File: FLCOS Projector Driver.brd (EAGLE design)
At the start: 73.9 x 62.1 mm, 62 parts, among them IC2 LM3414, IC3 MIC5219BM5, IC4 MIC5219BM5, IC5 LM3414, IC6 LM3414, Q1 14.31818MHz, Q3 12MHz, T2 S8050, T3 S8050, U1 TVP5150-NTSC_DECODER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

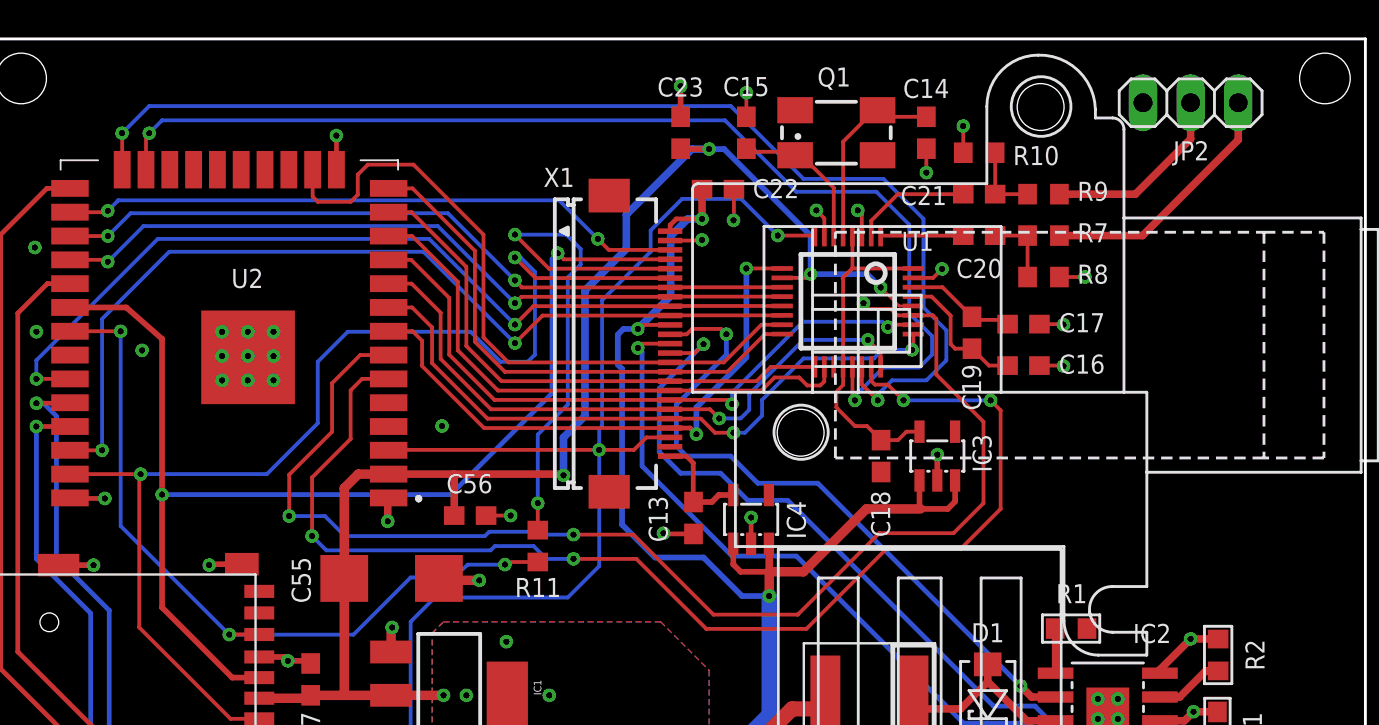
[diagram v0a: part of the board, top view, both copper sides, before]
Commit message: added pullups to I2C
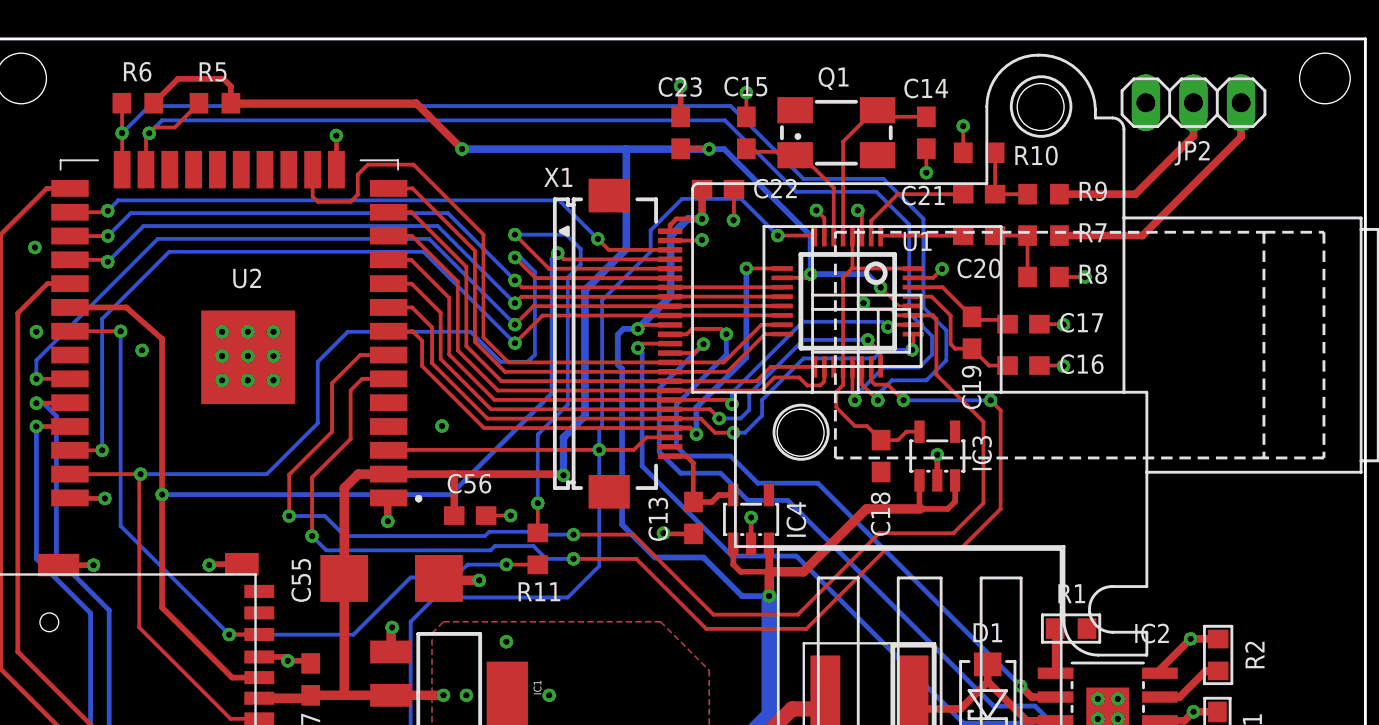
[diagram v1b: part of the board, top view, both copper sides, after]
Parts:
- added R5, R6: 2K2, rcl:R0603
- moved JP2 0.15 mm to (69.1, 62.5)
- moved R11 0.15 mm to (34.1, 38.7), turned to 90 degrees
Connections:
- net +3V3: now also R5.2, R6.2
- net FLCOS_SOUT: now also R11.2; no longer R11.1
- net SPI_MISO: now also R11.1; no longer R11.2
- net TVP_SCL: now also R5.1
- net TVP_SDA: now also R6.1
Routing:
- net +3V3: track 79.9 -> 109.8 mm, vias 9 -> 10
- net TVP_SCL: track 59.8 -> 63.0 mm
- net TVP_SDA: track 62.7 -> 64.3 mm
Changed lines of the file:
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@@
 <attribute name="OC_NEWARK" value="unknown" x="50.0634" y="60.9092" size="1.778" layer="27" display="off"/>
 </element>
-<element name="JP2" library="pinhead" package="1X03" package3d_urn="urn:adsk.eagle:package:22458/2" value="" x="68.961" y="62.5094" smashed="yes" rot="R180">
-<attribute name="NAME" x="69.9516" y="60.452" size="1.016" layer="25" ratio="10" rot="R180"/>
-<attribute name="VALUE" x="72.771" y="65.6844" size="1.27" layer="27" rot="R180"/>
+<element name="JP2" library="pinhead" package="1X03" package3d_urn="urn:adsk.eagle:package:22458/2" value="" x="69.1134" y="62.5094" smashed="yes" rot="R180">
+<attribute name="NAME" x="70.104" y="60.452" size="1.016" layer="25" ratio="10" rot="R180"/>
+<attribute name="VALUE" x="72.9234" y="65.6844" size="1.27" layer="27" rot="R180"/>
 </element>
 <element name="C22" library="rcl" package="C0603" value="100nF" x="43.7506" y="57.8984" smashed="yes" rot="R180">
@@
 <attribute name="VALUE" x="43.6118" y="37.1094" size="1.016" layer="27"/>
 </element>
-<element name="R11" library="rcl" package="R0603" value="0R" x="34.1376" y="38.862" smashed="yes" rot="R270">
-<attribute name="NAME" x="35.3822" y="37.1602" size="1.016" layer="25" rot="R180"/>
-<attribute name="VALUE" x="32.2326" y="39.497" size="1.27" layer="27" rot="R270"/>
-</element>
 <element name="IC1" library="SparkFun" package="SOT223" value="" x="29.4132" y="30.9" rot="R270"/>
 <element name="RGB" library="con-jst" package="ZH-8" value="ZH-8" x="39.0144" y="18.161" smashed="yes" rot="R270">
@@
 <attribute name="NAME" x="67.2846" y="15.554" size="1.016" layer="25" ratio="12" align="bottom-center"/>
 <attribute name="VALUE" x="64.5414" y="14.9444" size="0.5" layer="27" font="vector" ratio="12" rot="R180" align="top-center"/>
+</element>
+<element name="R11" library="rcl" package="R0603" value="0R" x="34.1376" y="38.7096" smashed="yes" rot="R90">
+<attribute name="NAME" x="35.4584" y="36.9316" size="1.016" layer="25" rot="R180"/>
+<attribute name="VALUE" x="36.0426" y="38.0746" size="1.27" layer="27" rot="R90"/>
+</element>
+<element name="R5" library="rcl" package="R0603" value="2K2" x="16.9164" y="62.484" smashed="yes">
+<attribute name="NAME" x="15.9766" y="63.6524" size="1.016" layer="25"/>
+<attribute name="VALUE" x="16.2814" y="60.579" size="1.27" layer="27"/>
+</element>
+<element name="R6" library="rcl" package="R0603" value="2K2" x="12.8016" y="62.484" smashed="yes">
+<attribute name="NAME" x="11.938" y="63.6524" size="1.016" layer="25"/>
+<attribute name="VALUE" x="12.1666" y="60.579" size="1.27" layer="27"/>
 </element>
 </elements>
@@
 <wire x1="50.923" y1="46.7654" x2="51.054" y2="46.6344" width="0.2032" layer="1"/>
 <via x="51.054" y="46.6344" extent="1-16" drill="0.3302"/>
-<wire x1="13.239" y1="58.9392" x2="13.239" y2="60.864" width="0.2032" layer="1"/>
-<wire x1="13.239" y1="60.864" x2="13.4112" y2="60.8838" width="0.2032" layer="1"/>
+<wire x1="13.239" y1="58.9392" x2="13.239" y2="60.7116" width="0.2032" layer="1"/>
+<wire x1="13.239" y1="60.7116" x2="13.4112" y2="60.8838" width="0.2032" layer="1"/>
 <via x="13.4112" y="60.8838" extent="1-16" drill="0.3302"/>
 <wire x1="52.197" y1="57.7596" x2="47.9298" y2="57.7596" width="0.2032" layer="16"/>
@@
 <wire x1="54.483" y1="48.387" x2="52.578" y2="48.387" width="0.2032" layer="16"/>
 <wire x1="52.578" y1="48.387" x2="51.054" y2="46.863" width="0.2032" layer="16"/>
+<contactref element="R5" pad="1"/>
+<wire x1="13.4112" y1="60.8838" x2="13.716" y2="61.1886" width="0.2032" layer="1"/>
+<wire x1="13.716" y1="61.1886" x2="14.771" y2="61.1886" width="0.2032" layer="1"/>
+<wire x1="14.771" y1="61.1886" x2="16.0664" y2="62.484" width="0.2032" layer="1"/>
 </signal>
 <signal name="TVP_SDA">
@@
 <wire x1="54.864" y1="47.7012" x2="53.0352" y2="47.7012" width="0.2032" layer="16"/>
 <wire x1="53.0352" y1="47.7012" x2="52.2732" y2="46.9392" width="0.2032" layer="16"/>
+<contactref element="R6" pad="1"/>
+<wire x1="11.9634" y1="60.8838" x2="11.9634" y2="62.4722" width="0.2032" layer="1"/>
+<wire x1="11.9634" y1="62.4722" x2="11.9516" y2="62.484" width="0.2032" layer="1"/>
 </signal>
 <signal name="XTAL1">
@@
 <via x="32.9184" y="55.4736" extent="1-16" drill="0.3302"/>
 <via x="34.1376" y="41.148" extent="1-16" drill="0.3302"/>
-<contactref element="R11" pad="1"/>
 <wire x1="34.735" y1="53.657" x2="32.9184" y2="55.4736" width="0.2032" layer="1"/>
 <wire x1="41.1976" y1="53.657" x2="34.735" y2="53.657" width="0.2032" layer="1"/>
 <wire x1="32.9184" y1="55.4736" x2="35.6616" y2="55.4736" width="0.2032" layer="16"/>
 <wire x1="36.4236" y1="54.7116" x2="35.6616" y2="55.4736" width="0.2032" layer="16"/>
-<wire x1="34.1376" y1="39.712" x2="34.1376" y2="41.148" width="0.2032" layer="1"/>
 <wire x1="36.4236" y1="53.8734" x2="36.4236" y2="54.7116" width="0.2032" layer="16"/>
 <wire x1="35.7378" y1="53.1876" x2="35.7378" y2="46.4058" width="0.2032" layer="16"/>
@@
 <wire x1="35.7378" y1="46.4058" x2="34.1376" y2="44.8056" width="0.2032" layer="16"/>
 <wire x1="34.1376" y1="44.8056" x2="34.1376" y2="41.148" width="0.2032" layer="16"/>
+<contactref element="R11" pad="2"/>
+<wire x1="34.1376" y1="39.5596" x2="34.1376" y2="41.148" width="0.2032" layer="1"/>
 </signal>
 <signal name="SPI_MOSI">
@@
 <contactref element="JP2" pad="1"/>
 <wire x1="61.9624" y1="55.4228" x2="66.3956" y2="55.4228" width="0.4064" layer="1"/>
-<wire x1="71.501" y1="60.5282" x2="71.501" y2="62.5094" width="0.4064" layer="1"/>
-<wire x1="66.3956" y1="55.4228" x2="71.501" y2="60.5282" width="0.4064" layer="1"/>
+<wire x1="71.6534" y1="60.6806" x2="71.6534" y2="62.5094" width="0.4064" layer="1"/>
+<wire x1="66.3956" y1="55.4228" x2="71.6534" y2="60.6806" width="0.4064" layer="1"/>
 </signal>
 <signal name="N$21">
@@
 <contactref element="JP2" pad="2"/>
 <wire x1="61.9624" y1="57.6326" x2="66.0146" y2="57.6326" width="0.4064" layer="1"/>
-<wire x1="68.961" y1="60.579" x2="68.961" y2="62.5094" width="0.4064" layer="1"/>
-<wire x1="66.0146" y1="57.6326" x2="68.961" y2="60.579" width="0.4064" layer="1"/>
+<wire x1="69.1134" y1="60.7314" x2="69.1134" y2="62.5094" width="0.4064" layer="1"/>
+<wire x1="66.0146" y1="57.6326" x2="69.1134" y2="60.7314" width="0.4064" layer="1"/>
 </signal>
 <signal name="+3V3">
@@
 <wire x1="33.8582" y1="23.872559375" x2="33.8582" y2="26.7208" width="0.2032" layer="1"/>
 <wire x1="33.8582" y1="26.7208" x2="32.5374" y2="28.0416" width="0.2032" layer="1"/>
-<wire x1="43.2816" y1="60.0354" x2="42.357" y2="60.0354" width="0.4064" layer="16"/>
 <wire x1="36.6522" y1="45.7962" x2="35.5092" y2="44.6532" width="0.4064" layer="16"/>
 <wire x1="35.5092" y1="44.6532" x2="35.5092" y2="42.633" width="0.4064" layer="16"/>
 <via x="35.5092" y="42.633" extent="1-16" drill="0.3302"/>
-<wire x1="42.357" y1="60.0354" x2="38.862" y2="56.5404" width="0.4064" layer="16"/>
-<wire x1="38.862" y1="56.5404" x2="38.862" y2="54.7116" width="0.4064" layer="16"/>
-<wire x1="38.862" y1="54.7116" x2="36.6522" y2="52.5018" width="0.4064" layer="16"/>
+<wire x1="36.6522" y1="52.5018" x2="38.862" y2="54.7116" width="0.4064" layer="16"/>
 <wire x1="36.6522" y1="52.5018" x2="36.6522" y2="45.7962" width="0.4064" layer="16"/>
 <wire x1="26.184" y1="42.6992" x2="29.6418" y2="42.6992" width="0.4064" layer="1"/>
@@
 <wire x1="29.6808" y1="40.4876" x2="29.6808" y2="42.6602" width="0.4064" layer="1"/>
 <wire x1="29.6808" y1="42.6602" x2="29.6418" y2="42.6992" width="0.4064" layer="1"/>
+<contactref element="R5" pad="2"/>
+<contactref element="R6" pad="2"/>
+<wire x1="17.7664" y1="63.3866" x2="17.7664" y2="62.484" width="0.3048" layer="1"/>
+<wire x1="17.7664" y1="63.3866" x2="17.3736" y2="63.7794" width="0.3048" layer="1"/>
+<wire x1="17.3736" y1="63.7794" x2="14.947" y2="63.7794" width="0.3048" layer="1"/>
+<wire x1="14.947" y1="63.7794" x2="13.6516" y2="62.484" width="0.3048" layer="1"/>
+<via x="30.099" y="60.0354" extent="1-16" drill="0.3302"/>
+<wire x1="43.2816" y1="60.0354" x2="38.862" y2="60.0354" width="0.4064" layer="16"/>
+<wire x1="38.862" y1="60.0354" x2="30.099" y2="60.0354" width="0.4064" layer="16"/>
+<wire x1="38.862" y1="54.7116" x2="38.862" y2="60.0354" width="0.4064" layer="16"/>
+<wire x1="27.6504" y1="62.484" x2="30.099" y2="60.0354" width="0.4064" layer="1"/>
+<wire x1="17.7664" y1="62.484" x2="27.6504" y2="62.484" width="0.4064" layer="1"/>
 </signal>
 <signal name="MOTOR">
@@
 <via x="17.6784" y="34.1376" extent="1-16" drill="0.3302"/>
 <via x="11.8872" y="50.3192" extent="1-16" drill="0.3302"/>
-<contactref element="R11" pad="2"/>
 <wire x1="9.184" y1="50.3192" x2="11.8872" y2="50.3192" width="0.2032" layer="1"/>
 <wire x1="11.8872" y1="39.9288" x2="11.8872" y2="50.3192" width="0.2032" layer="16"/>
 <wire x1="17.6784" y1="34.1376" x2="11.8872" y2="39.9288" width="0.2032" layer="16"/>
-<via x="32.385" y="37.8714" extent="1-16" drill="0.3302"/>
-<wire x1="32.385" y1="37.8714" x2="32.5492" y2="38.012" width="0.2032" layer="1"/>
-<wire x1="32.5492" y1="38.012" x2="34.1376" y2="38.012" width="0.2032" layer="1"/>
+<via x="32.4612" y="37.8714" extent="1-16" drill="0.3302"/>
 <wire x1="27.3558" y1="37.1856" x2="29.6418" y2="37.1856" width="0.2032" layer="16"/>
 <wire x1="29.6418" y1="37.1856" x2="30.4038" y2="37.8714" width="0.2032" layer="16"/>
 <wire x1="17.6784" y1="34.1376" x2="24.3078" y2="34.1376" width="0.2032" layer="16"/>
 <wire x1="24.3078" y1="34.1376" x2="27.3558" y2="37.1856" width="0.2032" layer="16"/>
-<wire x1="30.4038" y1="37.8714" x2="32.385" y2="37.8714" width="0.2032" layer="16"/>
+<wire x1="30.4038" y1="37.8714" x2="32.4612" y2="37.8714" width="0.2032" layer="16"/>
+<contactref element="R11" pad="1"/>
+<wire x1="32.4612" y1="37.8714" x2="34.1258" y2="37.8714" width="0.2032" layer="1"/>
+<wire x1="34.1258" y1="37.8714" x2="34.1376" y2="37.8596" width="0.2032" layer="1"/>
 </signal>
 <signal name="SD_CS_N">

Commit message: RGB LED current set to 156mA
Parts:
- R16, R2, R4: value 8K9 -> 20K
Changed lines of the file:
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@@
 <attribute name="VALUE" x="60.9356" y="25.6976" size="0.4064" layer="27" font="vector" ratio="12" rot="R270" align="top-center"/>
 </element>
-<element name="R16" library="A_butts" package="R0603" value="8K9" x="70.4228" y="24.0986" smashed="yes" rot="R270">
+<element name="R16" library="A_butts" package="R0603" value="20K" x="70.4228" y="24.0986" smashed="yes" rot="R270">
 <attribute name="NAME" x="71.7734" y="24.0652" size="1.016" layer="25" ratio="12" rot="R270" align="bottom-center"/>
 <attribute name="VALUE" x="70.4228" y="22.4486" size="0.4064" layer="27" font="vector" ratio="12" align="top-center"/>
@@
 <attribute name="VALUE" x="60.9356" y="34.4614" size="0.4064" layer="27" font="vector" ratio="12" rot="R270" align="top-center"/>
 </element>
-<element name="R2" library="A_butts" package="R0603" value="8K9" x="70.4286" y="33.0518" smashed="yes" rot="R270">
+<element name="R2" library="A_butts" package="R0603" value="20K" x="70.4286" y="33.0518" smashed="yes" rot="R270">
 <attribute name="NAME" x="71.8874" y="33.051" size="1.016" layer="25" ratio="12" rot="R270" align="bottom-center"/>
 <attribute name="VALUE" x="70.4286" y="31.4018" size="0.4064" layer="27" font="vector" ratio="12" align="top-center"/>
@@
 <attribute name="VALUE" x="60.9356" y="16.5838" size="0.4064" layer="27" font="vector" ratio="12" rot="R270" align="top-center"/>
 </element>
-<element name="R4" library="A_butts" package="R0603" value="8K9" x="70.355" y="15.1458" smashed="yes" rot="R270">
+<element name="R4" library="A_butts" package="R0603" value="20K" x="70.355" y="15.1458" smashed="yes" rot="R270">
 <attribute name="NAME" x="71.736" y="15.1414" size="1.016" layer="25" ratio="12" rot="R270" align="bottom-center"/>
 <attribute name="VALUE" x="70.355" y="13.4958" size="0.4064" layer="27" font="vector" ratio="12" align="top-center"/>

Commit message: schematic tweaks
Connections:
- net D0 renamed FLCOS_D0
- net D1 renamed FLCOS_D1
- net D2 renamed FLCOS_D2
- net D3 renamed FLCOS_D3
- net D4 renamed FLCOS_D4
- net D5 renamed FLCOS_D5
- net D6 renamed FLCOS_D6
- net D7 renamed FLCOS_D7
- net HD renamed FLCOS_HD
- net PCLK renamed FLCOS_PCLK
- net VALID renamed FLCOS_VALID
- net VD renamed FLCOS_VD
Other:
- board text added: "ElectronAsh, Oct 2022"
- board text added: "FLCOS Mini Projector v1.0"
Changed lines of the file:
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@@
 <vertex x="-215.09355" y="-223.8756"/>
 </polygon>
+<text x="74.9046" y="13.7922" size="1.016" layer="21" rot="R90">FLCOS Mini Projector v1.0</text>
+<text x="76.3524" y="15.8496" size="0.8128" layer="21" rot="R90">ElectronAsh, Oct 2022</text>
 </plain>
 <attributes>
@@
 <attribute name="VALUE" x="43.6118" y="37.1094" size="1.016" layer="27"/>
 </element>
-<element name="IC1" library="SparkFun" package="SOT223" value="" x="29.4132" y="30.9" rot="R270"/>
+<element name="IC1" library="SparkFun" package="SOT223" value="" x="29.4132" y="30.9" smashed="yes" rot="R270">
+<attribute name="NAME" x="34.1503" y="31.9541" size="1.016" layer="25" rot="R270"/>
+<attribute name="VALUE" x="29.2227" y="31.9795" size="0.4064" layer="27" rot="R270"/>
+</element>
 <element name="RGB" library="con-jst" package="ZH-8" value="ZH-8" x="39.0144" y="18.161" smashed="yes" rot="R270">
 <attribute name="NAME" x="36.7108" y="25.2744" size="1.27" layer="25"/>
@@
 <via x="32.6898" y="40.4876" extent="1-16" drill="0.3302"/>
 </signal>
-<signal name="D7">
+<signal name="FLCOS_D7">
 <contactref element="X1" pad="7"/>
 <contactref element="U1" pad="11"/>
@@
 <wire x1="29.337" y1="56.6166" x2="32.9184" y2="53.0352" width="0.2032" layer="16"/>
 </signal>
-<signal name="D6">
+<signal name="FLCOS_D6">
 <contactref element="X1" pad="8"/>
 <contactref element="U1" pad="12"/>
@@
 <wire x1="11.098" y1="54.1292" x2="11.2014" y2="54.0258" width="0.2032" layer="1"/>
 </signal>
-<signal name="D5">
+<signal name="FLCOS_D5">
 <contactref element="X1" pad="9"/>
 <contactref element="U1" pad="13"/>
@@
 <wire x1="28.3464" y1="55.245" x2="32.9184" y2="50.673" width="0.2032" layer="16"/>
 </signal>
-<signal name="D4">
+<signal name="FLCOS_D4">
 <contactref element="X1" pad="10"/>
 <contactref element="U1" pad="14"/>
@@
 <wire x1="43.8912" y1="42.7482" x2="41.7576" y2="42.7482" width="0.254" layer="16"/>
 </signal>
-<signal name="D3">
+<signal name="FLCOS_D3">
 <contactref element="X1" pad="15"/>
 <contactref element="U1" pad="15"/>
@@
 <wire x1="31.242" y1="55.4736" x2="27.5082" y2="59.2074" width="0.2032" layer="1"/>
 </signal>
-<signal name="D2">
+<signal name="FLCOS_D2">
 <contactref element="X1" pad="16"/>
 <contactref element="U1" pad="16"/>
@@
 <wire x1="30.7848" y1="49.7586" x2="30.7848" y2="54.6136" width="0.2032" layer="1"/>
 </signal>
-<signal name="D1">
+<signal name="FLCOS_D1">
 <contactref element="X1" pad="17"/>
 <contactref element="U1" pad="17"/>
@@
 <wire x1="30.3276" y1="49.53" x2="30.3276" y2="53.75" width="0.2032" layer="1"/>
 </signal>
-<signal name="D0">
+<signal name="FLCOS_D0">
 <contactref element="X1" pad="18"/>
 <contactref element="U1" pad="18"/>
@@
 <wire x1="46.76590625" y1="47.8536" x2="46.06930625" y2="47.157" width="0.2032" layer="1"/>
 </signal>
-<signal name="VALID">
+<signal name="FLCOS_VALID">
 <contactref element="X1" pad="19"/>
 <contactref element="U1" pad="26"/>
@@
 <wire x1="48.2854" y1="50.8254" x2="52.5272" y2="50.8254" width="0.2032" layer="16"/>
 </signal>
-<signal name="VD">
+<signal name="FLCOS_VD">
 <contactref element="X1" pad="20"/>
 <contactref element="U1" pad="24"/>
@@
 <wire x1="28.956" y1="48.8442" x2="28.956" y2="51.3116" width="0.2032" layer="1"/>
 </signal>
-<signal name="HD">
+<signal name="FLCOS_HD">
 <contactref element="X1" pad="21"/>
 <contactref element="U1" pad="25"/>
@@
 <wire x1="52.07" y1="48.8696" x2="52.5272" y2="49.3268" width="0.2032" layer="16"/>
 </signal>
-<signal name="PCLK">
+<signal name="FLCOS_PCLK">
 <contactref element="X1" pad="22"/>
 <contactref element="U1" pad="9"/>
@@
 <wire x1="17.6784" y1="34.1376" x2="11.8872" y2="39.9288" width="0.2032" layer="16"/>
 <via x="32.4612" y="37.8714" extent="1-16" drill="0.3302"/>
-<wire x1="27.3558" y1="37.1856" x2="29.6418" y2="37.1856" width="0.2032" layer="16"/>
-<wire x1="29.6418" y1="37.1856" x2="30.4038" y2="37.8714" width="0.2032" layer="16"/>
-<wire x1="17.6784" y1="34.1376" x2="24.3078" y2="34.1376" width="0.2032" layer="16"/>
-<wire x1="24.3078" y1="34.1376" x2="27.3558" y2="37.1856" width="0.2032" layer="16"/>
-<wire x1="30.4038" y1="37.8714" x2="32.4612" y2="37.8714" width="0.2032" layer="16"/>
+<wire x1="25.527" y1="37.338" x2="29.7942" y2="37.338" width="0.2032" layer="16"/>
+<wire x1="29.7942" y1="37.338" x2="30.3276" y2="37.8714" width="0.2032" layer="16"/>
+<wire x1="17.6784" y1="34.1376" x2="22.2504" y2="34.1376" width="0.2032" layer="16"/>
+<wire x1="22.2504" y1="34.1376" x2="25.527" y2="37.338" width="0.2032" layer="16"/>
+<wire x1="30.3276" y1="37.8714" x2="32.4612" y2="37.8714" width="0.2032" layer="16"/>
 <contactref element="R11" pad="1"/>
 <wire x1="32.4612" y1="37.8714" x2="34.1258" y2="37.8714" width="0.2032" layer="1"/>

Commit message: Allow USB/GPIO0 to reset TVP and FLCOS
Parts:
- moved R11 0.15 mm to (34.0, 38.7)
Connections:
- removed net EN_N: R67.1, T3.3, U1.8, U2.3, X1.23
- removed net GPIO0: T2.3, U2.25
- new net ESP_EN_N: R67.1, T3.3, U2.3
- new net TVP_FL_RST_N: T2.3, U1.8, U2.25, X1.23
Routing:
- net TVP_FL_RST_N: track 0.00 -> 111.4 mm, vias 0 -> 7
- net EN_N: track 74.2 -> 0.00 mm, vias 3 -> 0
- net GPIO0: track 48.7 -> 0.00 mm, vias 2 -> 0
- net ESP_EN_N: track 0.00 -> 44.6 mm, vias 0 -> 2
- net FLCOS_SOUT: track 29.0 -> 30.0 mm
- net +3V3: track 109.8 -> 108.8 mm
